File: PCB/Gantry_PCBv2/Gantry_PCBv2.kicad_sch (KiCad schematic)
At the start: 138 parts, among them J1 Conn_01x14, J10 B2B-XH-A_LF__SN_, J11 B2B-XH-A_LF__SN_, J12 B2B-XH-A_LF__SN_, J14 USB_C_Receptacle_USB2.0_16P, J15 Conn_01x03_Pin, J17 B2B-XH-A_LF__SN_, J2 Conn_01x14, J3 Conn_01x10, J4 Screw_Terminal_01x02, J5 DCJ200-10-A-XX-X_REVA, J6 Conn_01x04_Pin, J7 Conn_01x04_Pin, J8 Conn_01x04_Pin, J9 Conn_01x04_Pin, Q1 SS8050, Q2 SS8050, Q3 NMOS, SW7 SW_0, SW8 SW_EN, U1 ESP32-WROOM-32E, U10 TLV75733PDBV, U11 74HC245, U2 CH340C, U3 TB6612FNG H-bridge Motor Driv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, U4 MP1584, U5 74HC245, U6 DRV8825_STEPPER_MOTOR_DRIVER_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, U7 DRV8825_STEPPER_MOTOR_DRIVER_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, U8 DRV8825_STEPPER_MOTOR_DRIVER_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, U9 DRV8825_STEPPER_MOTOR_DRIVER_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

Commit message: schematic updates
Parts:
- C10: renamed from C19; footprint (none) -> Capacitor_SMD:C_0805_2012Metric
- C11: renamed from C20; footprint (none) -> Capacitor_SMD:C_01005_0402Metric
- C12: renamed from C17; footprint (none) -> Capacitor_SMD:C_01005_0402Metric
- D10: renamed from D16; footprint (none) -> LED_SMD:LED_0201_0603Metric_Pad0.64x0.40mm_HandSolder
- D11: renamed from D3; footprint (none) -> LED_SMD:LED_0201_0603Metric_Pad0.64x0.40mm_HandSolder
- D13: renamed from D9; footprint (none) -> LED_SMD:LED_0201_0603Metric_Pad0.64x0.40mm_HandSolder
- D14: renamed from D10; footprint (none) -> LED_SMD:LED_0201_0603Metric_Pad0.64x0.40mm_HandSolder
- D15: renamed from D11; footprint (none) -> LED_SMD:LED_0201_0603Metric_Pad0.64x0.40mm_HandSolder
- D16: renamed from D12; footprint (none) -> LED_SMD:LED_0201_0603Metric_Pad0.64x0.40mm_HandSolder
- D17: footprint (none) -> LED_SMD:LED_0201_0603Metric_Pad0.64x0.40mm_HandSolder
- D6: renamed from D13; footprint (none) -> LED_SMD:LED_0201_0603Metric_Pad0.64x0.40mm_HandSolder
- D7: renamed from D14; footprint (none) -> LED_SMD:LED_0201_0603Metric_Pad0.64x0.40mm_HandSolder
- D8: renamed from D15; footprint (none) -> LED_SMD:LED_0201_0603Metric_Pad0.64x0.40mm_HandSolder
- R13: renamed from R14; footprint (none) -> Resistor_SMD:R_0805_2012Metric_Pad1.20x1.40mm_HandSolder
- R14: renamed from R16; footprint (none) -> Resistor_SMD:R_0805_2012Metric_Pad1.20x1.40mm_HandSolder
- R15: renamed from R6; footprint (none) -> Resistor_SMD:R_0805_2012Metric_Pad1.20x1.40mm_HandSolder
- R16: renamed from R15; footprint (none) -> Resistor_SMD:R_0805_2012Metric_Pad1.20x1.40mm_HandSolder
- R17, TH1: footprint (none) -> Resistor_SMD:R_0805_2012Metric_Pad1.20x1.40mm_HandSolder
- R18: renamed from R7; footprint (none) -> Resistor_SMD:R_0805_2012Metric_Pad1.20x1.40mm_HandSolder
- R6: renamed from R40; footprint (none) -> Resistor_SMD:R_0815_2038Metric
- TP1: renamed from TP7; footprint (none) -> TestPoint:TestPoint_Pad_D2.0mm
- TP2: renamed from TP8; footprint (none) -> TestPoint:TestPoint_Pad_D2.0mm
- TP3: renamed from TP1; footprint (none) -> TestPoint:TestPoint_Pad_D2.0mm
- TP4: renamed from TP2; footprint (none) -> TestPoint:TestPoint_Pad_D2.0mm
- TP5: renamed from TP3; footprint (none) -> TestPoint:TestPoint_Pad_D2.0mm
- TP6: renamed from TP4; footprint (none) -> TestPoint:TestPoint_Pad_D2.0mm
- TP7: renamed from TP5; footprint (none) -> TestPoint:TestPoint_Pad_D2.0mm
- TP8: renamed from TP6; footprint (none) -> TestPoint:TestPoint_Pad_D2.0mm
- renumbered C22 to C13, C4 to C14, C23 to C15, C24 to C16, C5 to C17, C16 to C18, C13 to C19, C6 to C2, C15 to C20, C14 to C21, C9 to C22, C11 to C23, C8 to C24, C10 to C25, C12 to C26, C25 to C27, C6 to C3, C7 to C4, C2 to C5, C7 to C6, C3 to C7, C21 to C8, C18 to C9, D7 to D1, D6 to D12, D8 to D2, D8 to D3, D5 to D4, D7 to D5, D4 to D9, F2 to F1, F1 to F3, H5 to H1, H6 to H2, H7 to H3, H8 to H4, H1 to H5, H2 to H6, H3 to H7, H4 to H8, J4 to J1, J17 to J10, J14 to J11, J6 to J12, J7 to J13, J8 to J14, J9 to J15, J5 to J2, J15 to J3, J1 to J4, J10 to J5, J11 to J6, J12 to J7, J2 to J8, J3 to J9, Q3 to Q1, Q1 to Q2, Q2 to Q3, R49 to R10, R22 to R11, R23 to R12, R4 to R19, R18 to R2, R5 to R20, R29 to R21, R30 to R22, R13 to R23, R36 to R25, R37 to R26, R31 to R27, R10 to R28, R11 to R29, R19 to R3, R32 to R30, R33 to R31, R12 to R32, R8 to R33, R9 to R34, R25 to R35, R38 to R36, R39 to R37, R34 to R38, R35 to R39, R20 to R4, R26 to R40, R27 to R41, R28 to R42, R21 to R5, R50 to R7, R2 to R8, R3 to R9, SW7 to SW1, SW8 to SW2, U5 to U10, U4 to U2, U2 to U3, U10 to U4, U8 to U5, U9 to U6, U3 to U7, U6 to U8, U7 to U9
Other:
- moved on the sheet: C1, C10, C11, C12, C13, C14, C15, C16, C17, C18, C19, C2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

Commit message: Added Footprints and Formatting
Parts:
- F3: footprint (none) -> Fuse:Fuse_Littelfuse-LVR100
- Q1: footprint (none) -> Package_TO_SOT_THT:TO-247-3_Vertical
- U10, U11: footprint (none) -> Package_SO:SOIC-20W_7.5x15.4mm_P1.27mm
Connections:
- net 5V_R: now also U4.3 (EN)
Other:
- moved on the sheet: C13, C15, C16, C9, U4

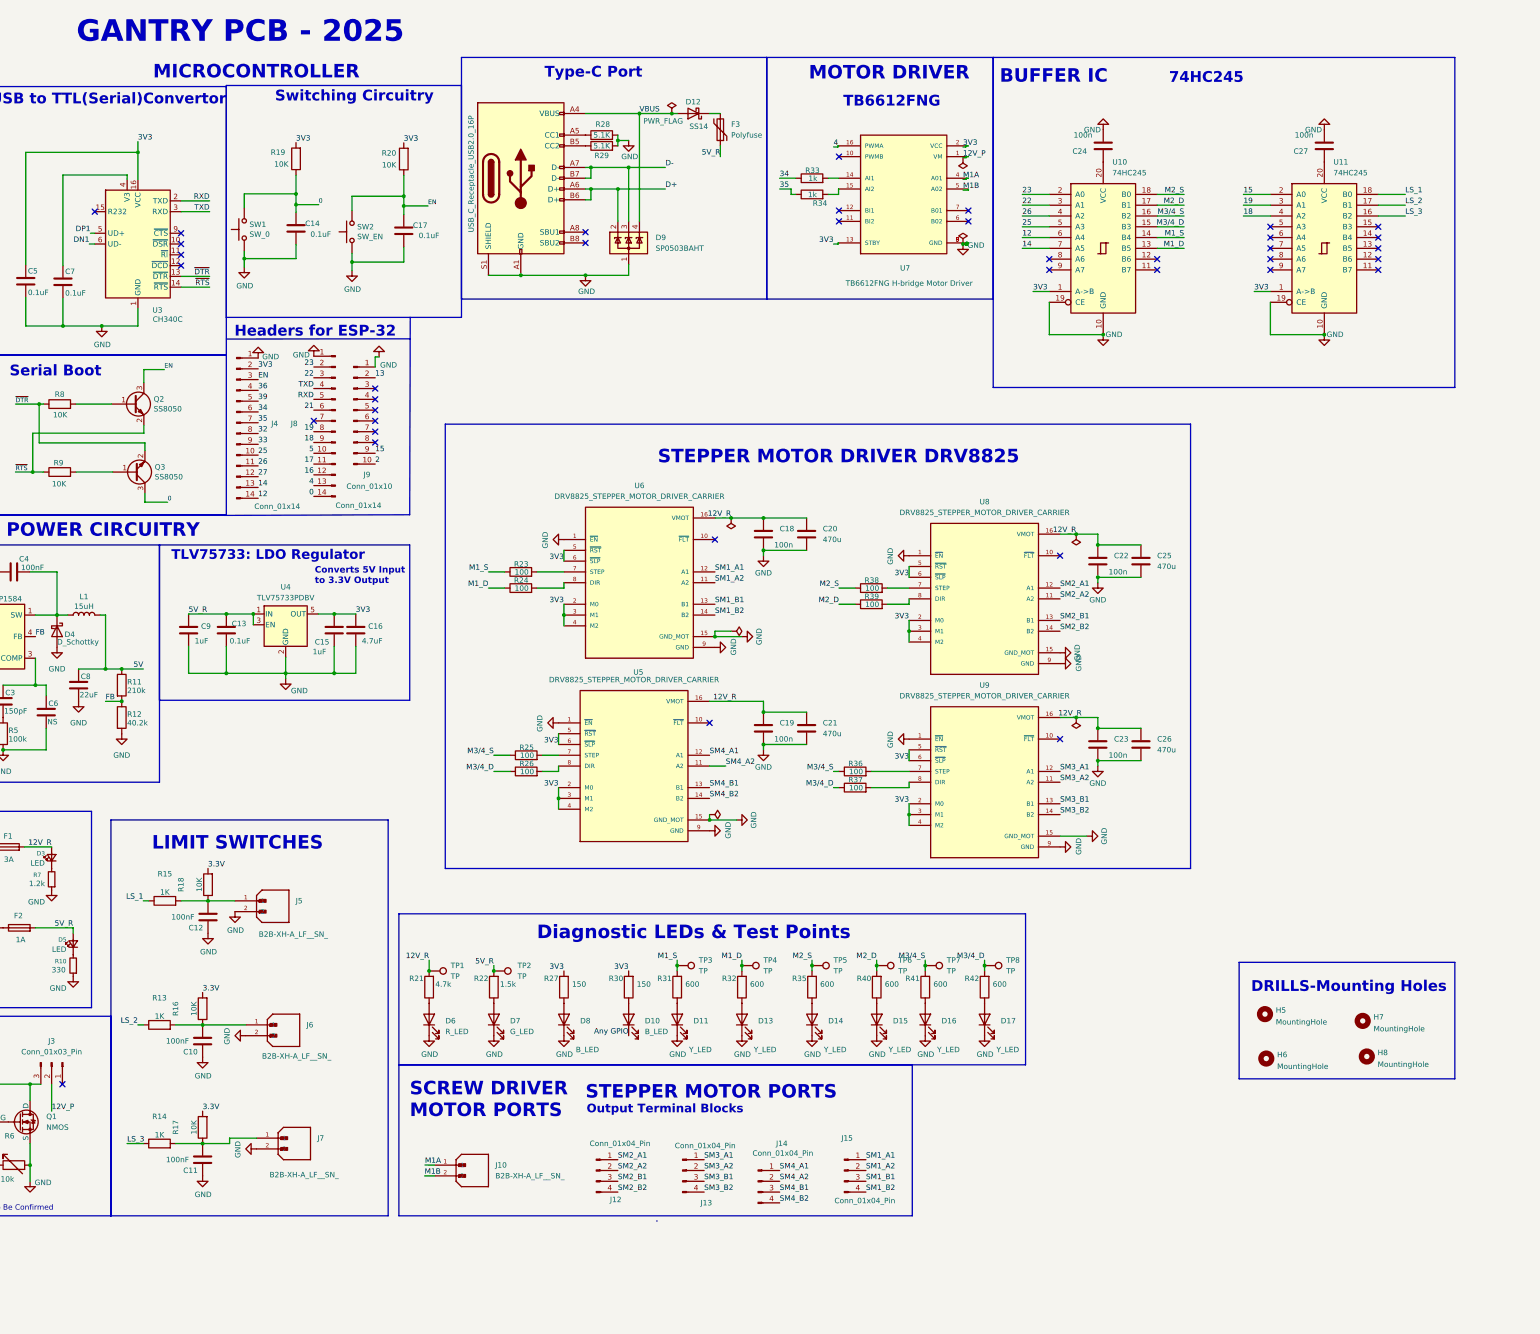
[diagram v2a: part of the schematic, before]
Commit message: Added MCP23017 GPIO Expander and Joystick
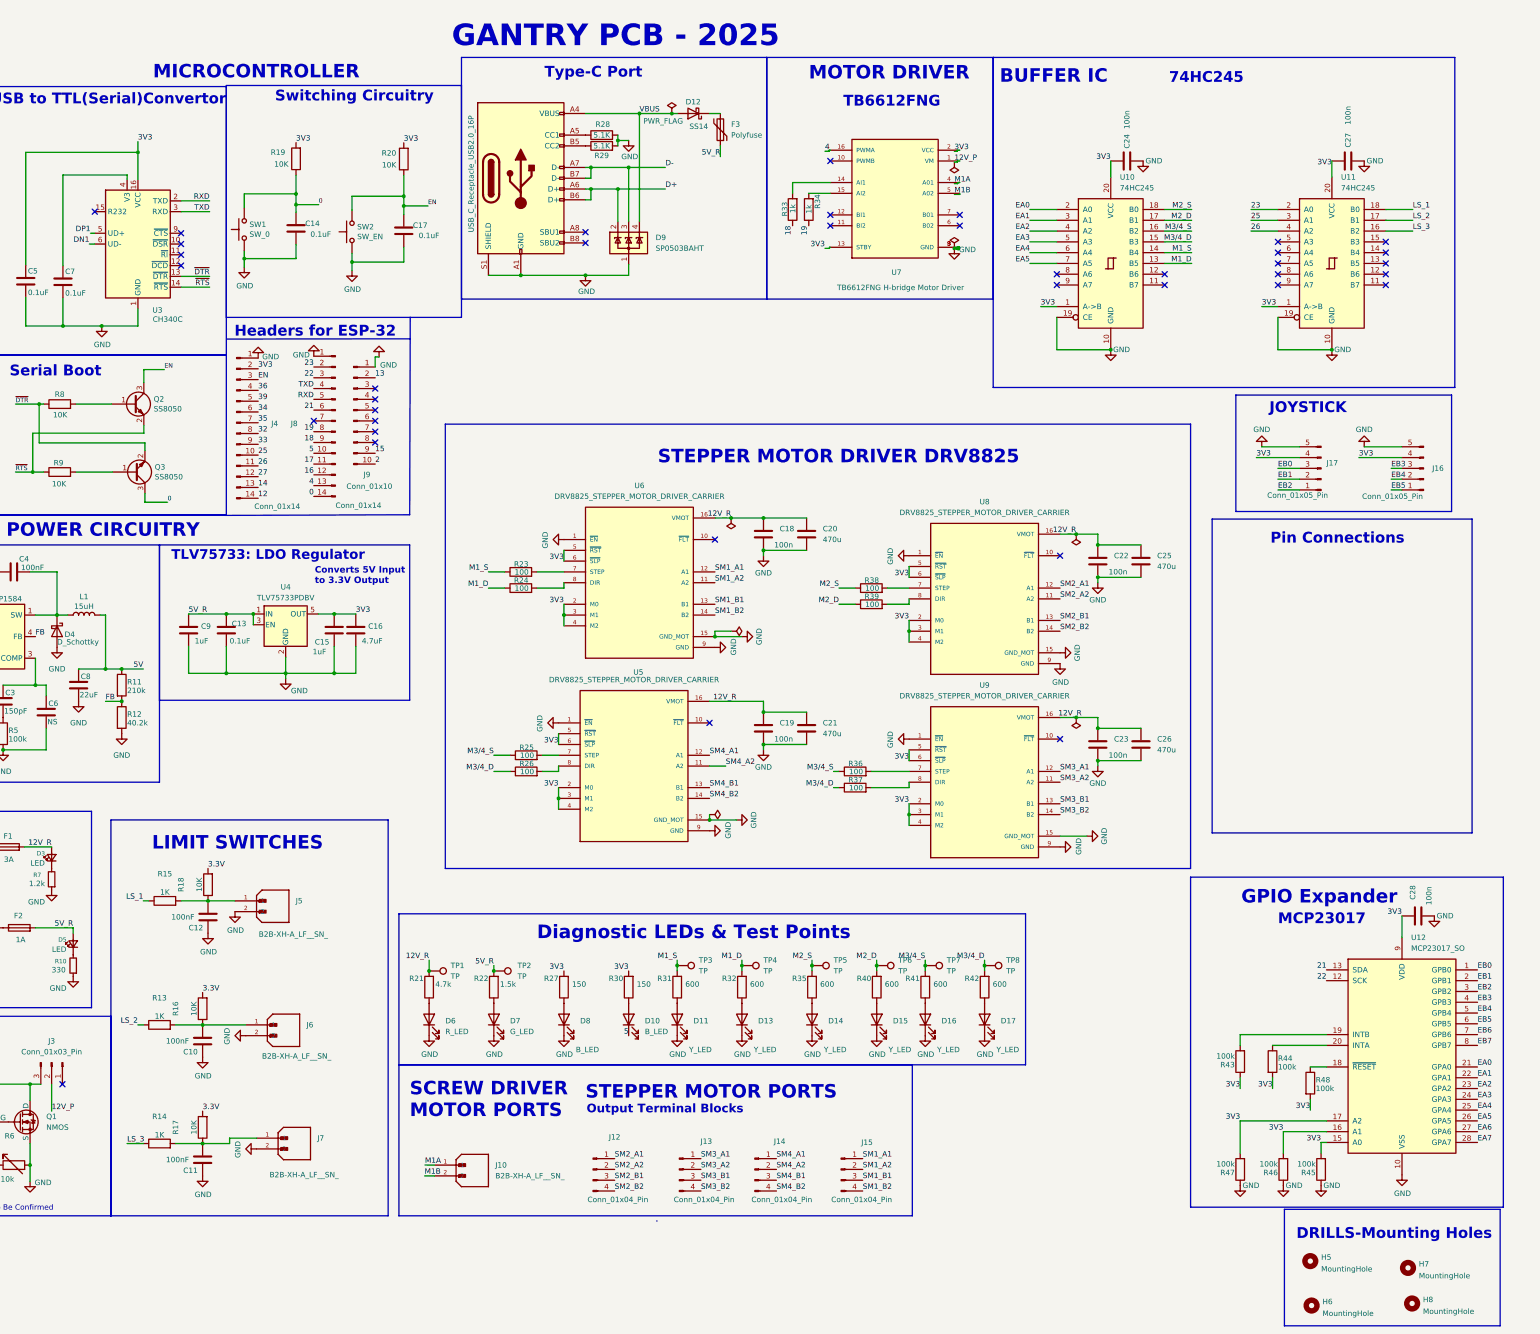
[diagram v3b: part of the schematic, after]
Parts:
- added C28: 100n, Capacitor_SMD:CP_Elec_6.3x7.7, symbol Device:C
- added J16, J17: Conn_01x05_Pin, Connector_PinHeader_2.54mm:PinHeader_1x05_P2.54mm_Vertical, symbol Connector:Conn_01x05_Pin
- added R43, R44, R45, R46, R47, R48: 100k, Resistor_SMD:R_0805_2012Metric_Pad1.20x1.40mm_HandSolder, symbol Device:R
- added U12: MCP23017_SO, Package_SO:SOIC-28W_7.5x17.9mm_P1.27mm, symbol Interface_Expansion:MCP23017_SO
- U1: footprint ESP32-WROOM:XCVR_ESP32-WROOM-32E__4MB_HIGH_TEMP_ -> RF_Module:ESP32-WROOM-32E
- U5, U6, U8, U9: footprint DRV8825_STEPPER_MOTOR_DRIVER_CARRIER (1):IC_DRV8825_STEPPER_MOTOR_DRIVER_CARRIER -> StepperMotor Driver:stepper
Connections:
- net Any GPIO is gone; now on net 5: D10.1 (K)
- net 12: no longer U10.6 (A4)
- net 14: no longer U10.7 (A5)
- net 15: no longer U11.2 (A0)
- net 18: now also R33.1; no longer U11.4 (A2)
- net 19: now also R34.1; no longer U11.3 (A1)
- net 21: now also U12.13 (SDA)
- net 22: now also U12.12 (SCK); no longer U10.3 (A1)
- net 23: now also U11.2 (A0); no longer U10.2 (A0)
- net 25: now also U11.3 (A1); no longer U10.5 (A3)
- net 26: now also U11.4 (A2); no longer U10.4 (A2)
- net 34: no longer R33.1
- net 35: no longer R34.1
- net 3V3: now also C24.2, C27.2, U10.20 (VCC), U11.20 (VCC), C28.1, J16.4 (Pin_4), J17.4 (Pin_4), R43.1, R44.2, R45.2, R46.2, R47.2, R48.2, U12.15 (A0), U12.16 (A1), U12.17 (A2), U12.9 (VDD)
- net GND: now also C24.1, C27.1, C28.2, J16.5 (Pin_5), J17.5 (Pin_5), R45.1, R46.1, R47.1, U12.10 (VSS); no longer C24.2, C27.2
- new net: R43.2, U12.19 (INTB)
- new net: R48.1, U12.18 (~{RESET})
- new net: R44.1, U12.20 (INTA)
- new net EA0: U10.2 (A0), U12.21 (GPA0)
- new net EA1: U10.3 (A1), U12.22 (GPA1)
- new net EA2: U10.4 (A2), U12.23 (GPA2)
- new net EA3: U10.5 (A3), U12.24 (GPA3)
- new net EA4: U10.6 (A4), U12.25 (GPA4)
- new net EA5: U10.7 (A5), U12.26 (GPA5)
- new net EA6: U12.27 (GPA6)
- new net EA7: U12.28 (GPA7)
- new net EB0: J17.3 (Pin_3), U12.1 (GPB0)
- new net EB1: J17.2 (Pin_2), U12.2 (GPB1)
- new net EB2: J17.1 (Pin_1), U12.3 (GPB2)
- new net EB3: J16.3 (Pin_3), U12.4 (GPB3)
- new net EB4: J16.2 (Pin_2), U12.5 (GPB4)
- new net EB5: J16.1 (Pin_1), U12.6 (GPB5)
- new net EB6: U12.7 (GPB6)
- new net EB7: U12.8 (GPB7)
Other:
- note added: "GPIO Expander"
- note added: "JOYSTICK"
- note added: "MCP23017"
- note added: "Pin Connections"
- moved on the sheet: C24, C27, H5, H6, H7, H8, J12, J13, J14, J15, R33, R34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
